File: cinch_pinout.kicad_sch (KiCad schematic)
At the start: 3 parts, among them J1 Conn, J2 Pinout

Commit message: Changed resistor footprint
Enables now both: SMD or throughhole resistor
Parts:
- added R1T1: 1k, Resistor_THT:R_Axial_DIN0207_L6.3mm_D2.5mm_P10.16mm_Horizontal, symbol Device:R
- J2: footprint (none) -> Connector_PinHeader_2.54mm:PinHeader_1x03_P2.54mm_Vertical
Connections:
- net +3V3: now also R1T1.1
- net AIN: now also R1T1.2
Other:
- moved on the sheet: R1
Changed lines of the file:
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@@
     (company "chof.org")
   )
+  (junction (at 140.97 62.23) (diameter 0) (color 0 0 0 0)
+  )
+  (junction (at 137.16 73.66) (diameter 0) (color 0 0 0 0)
+  )
   (junction (at 180.34 77.47) (diameter 0) (color 0 0 0 0)
   )
   (junction (at 176.53 71.12) (diameter 0) (color 0 0 0 0)
   )
-  (junction (at 140.97 73.66) (diameter 0) (color 0 0 0 0)
+  (junction (at 144.78 73.66) (diameter 0) (color 0 0 0 0)
   )
   (junction (at 132.08 73.66) (diameter 0) (color 0 0 0 0)
   )
+  (wire (pts (xy 180.34 78.74) (xy 180.34 77.47))
+    (stroke (width 0) (type default) (color 0 0 0 0))
+  )
+  (wire (pts (xy 137.16 62.23) (xy 137.16 63.5))
+    (stroke (width 0) (type default) (color 0 0 0 0))
+  )
+  (wire (pts (xy 144.78 71.12) (xy 144.78 73.66))
+    (stroke (width 0) (type default) (color 0 0 0 0))
+  )
+  (wire (pts (xy 137.16 73.66) (xy 144.78 73.66))
+    (stroke (width 0) (type default) (color 0 0 0 0))
+  )
+  (wire (pts (xy 144.78 73.66) (xy 148.59 73.66))
+    (stroke (width 0) (type default) (color 0 0 0 0))
+  )
+  (wire (pts (xy 132.08 73.66) (xy 137.16 73.66))
+    (stroke (width 0) (type default) (color 0 0 0 0))
+  )
+  (wire (pts (xy 144.78 62.23) (xy 144.78 63.5))
+    (stroke (width 0) (type default) (color 0 0 0 0))
+  )
+  (wire (pts (xy 182.88 66.04) (xy 182.88 71.12))
+    (stroke (width 0) (type default) (color 0 0 0 0))
+  )
+  (wire (pts (xy 111.76 76.2) (xy 111.76 69.85))
+    (stroke (width 0) (type default) (color 0 0 0 0))
+  )
+  (wire (pts (xy 140.97 62.23) (xy 144.78 62.23))
+    (stroke (width 0) (type default) (color 0 0 0 0))
+  )
+  (wire (pts (xy 140.97 62.23) (xy 137.16 62.23))
+    (stroke (width 0) (type default) (color 0 0 0 0))
+  )
+  (wire (pts (xy 180.34 76.2) (xy 171.45 76.2))
+    (stroke (width 0) (type default) (color 0 0 0 0))
+  )
+  (wire (pts (xy 134.62 76.2) (xy 134.62 92.71))
+    (stroke (width 0) (type default) (color 0 0 0 0))
+  )
+  (wire (pts (xy 132.08 69.85) (xy 132.08 73.66))
+    (stroke (width 0) (type default) (color 0 0 0 0))
+  )
+  (wire (pts (xy 176.53 71.12) (xy 171.45 71.12))
+    (stroke (width 0) (type default) (color 0 0 0 0))
+  )
+  (wire (pts (xy 111.76 69.85) (xy 132.08 69.85))
+    (stroke (width 0) (type default) (color 0 0 0 0))
+  )
   (wire (pts (xy 132.08 76.2) (xy 134.62 76.2))
     (stroke (width 0) (type default) (color 0 0 0 0))
   )
-  (wire (pts (xy 180.34 78.74) (xy 180.34 77.47))
-    (stroke (width 0) (type default) (color 0 0 0 0))
-  )
-  (wire (pts (xy 140.97 71.12) (xy 140.97 73.66))
-    (stroke (width 0) (type default) (color 0 0 0 0))
-  )
-  (wire (pts (xy 140.97 73.66) (xy 144.78 73.66))
-    (stroke (width 0) (type default) (color 0 0 0 0))
-  )
-  (wire (pts (xy 140.97 62.23) (xy 140.97 63.5))
-    (stroke (width 0) (type default) (color 0 0 0 0))
-  )
-  (wire (pts (xy 182.88 66.04) (xy 182.88 71.12))
-    (stroke (width 0) (type default) (color 0 0 0 0))
-  )
-  (wire (pts (xy 111.76 76.2) (xy 111.76 69.85))
-    (stroke (width 0) (type default) (color 0 0 0 0))
-  )
-  (wire (pts (xy 137.16 62.23) (xy 140.97 62.23))
-    (stroke (width 0) (type default) (color 0 0 0 0))
-  )
-  (wire (pts (xy 180.34 76.2) (xy 171.45 76.2))
-    (stroke (width 0) (type default) (color 0 0 0 0))
-  )
-  (wire (pts (xy 134.62 76.2) (xy 134.62 92.71))
-    (stroke (width 0) (type default) (color 0 0 0 0))
-  )
-  (wire (pts (xy 132.08 69.85) (xy 132.08 73.66))
-    (stroke (width 0) (type default) (color 0 0 0 0))
-  )
-  (wire (pts (xy 176.53 71.12) (xy 171.45 71.12))
-    (stroke (width 0) (type default) (color 0 0 0 0))
-  )
-  (wire (pts (xy 132.08 73.66) (xy 140.97 73.66))
-    (stroke (width 0) (type default) (color 0 0 0 0))
-  )
-  (wire (pts (xy 111.76 69.85) (xy 132.08 69.85))
-    (stroke (width 0) (type default) (color 0 0 0 0))
-  )
   (wire (pts (xy 182.88 71.12) (xy 176.53 71.12))
     (stroke (width 0) (type default) (color 0 0 0 0))
@@
   )
   (wire (pts (xy 180.34 77.47) (xy 180.34 76.2))
+    (stroke (width 0) (type default) (color 0 0 0 0))
+  )
+  (wire (pts (xy 137.16 71.12) (xy 137.16 73.66))
     (stroke (width 0) (type default) (color 0 0 0 0))
   )
@@
     )
   )
-  (global_label "AIN" (shape output) (at 144.78 73.66 0) (fields_autoplaced)
+  (global_label "AIN" (shape output) (at 148.59 73.66 0) (fields_autoplaced)
     (effects (font (size 1.27 1.27)) (justify left))
-    (property "Intersheet References" "${INTERSHEET_REFS}" (id 0) (at 150.2169 73.5806 0)
-      (effects (font (size 1.27 1.27)) (justify left) hide)
-    )
-  )
-  (symbol (lib_id "power:+3.3V") (at 137.16 62.23 0) (unit 1)
-    (in_bom yes) (on_board yes) (fields_autoplaced)
-    (property "Reference" "#PWR02" (id 0) (at 137.16 66.04 0)
-      (effects (font (size 1.27 1.27)) hide)
-    )
-    (property "Value" "+3.3V" (id 1) (at 137.16 57.15 0))
-    (property "Footprint" "" (id 2) (at 137.16 62.23 0)
-      (effects (font (size 1.27 1.27)) hide)
-    )
-    (property "Datasheet" "" (id 3) (at 137.16 62.23 0)
+    (property "Intersheet References" "${INTERSHEET_REFS}" (id 0) (at 154.0269 73.5806 0)
+      (effects (font (size 1.27 1.27)) (justify left) hide)
+    )
+  )
+  (symbol (lib_id "power:+3.3V") (at 140.97 62.23 0) (unit 1)
+    (in_bom yes) (on_board yes) (fields_autoplaced)
+    (property "Reference" "#PWR02" (id 0) (at 140.97 66.04 0)
+      (effects (font (size 1.27 1.27)) hide)
+    )
+    (property "Value" "+3.3V" (id 1) (at 140.97 57.15 0))
+    (property "Footprint" "" (id 2) (at 140.97 62.23 0)
+      (effects (font (size 1.27 1.27)) hide)
+    )
+    (property "Datasheet" "" (id 3) (at 140.97 62.23 0)
       (effects (font (size 1.27 1.27)) hide)
     )
@@
     (pin "1")
   )
-  (symbol (lib_id "Device:R") (at 140.97 67.31 0) (unit 1)
-    (in_bom yes) (on_board yes) (fields_autoplaced)
-    (property "Reference" "R1" (id 0) (at 143.51 66.0399 0)
-      (effects (font (size 1.27 1.27)) (justify left))
-    )
-    (property "Value" "1k" (id 1) (at 143.51 68.5799 0)
-      (effects (font (size 1.27 1.27)) (justify left))
-    )
-    (property "Footprint" "Resistor_SMD:R_0603_1608Metric_Pad0.98x0.95mm_HandSolder" (id 2) (at 139.192 67.31 90)
-      (effects (font (size 1.27 1.27)) hide)
-    )
-    (property "Datasheet" "~" (id 3) (at 140.97 67.31 0)
+  (symbol (lib_id "Device:R") (at 144.78 67.31 0) (unit 1)
+    (in_bom yes) (on_board yes) (fields_autoplaced)
+    (property "Reference" "R1" (id 0) (at 147.32 66.0399 0)
+      (effects (font (size 1.27 1.27)) (justify left))
+    )
+    (property "Value" "1k" (id 1) (at 147.32 68.5799 0)
+      (effects (font (size 1.27 1.27)) (justify left))
+    )
+    (property "Footprint" "Resistor_SMD:R_0603_1608Metric_Pad0.98x0.95mm_HandSolder" (id 2) (at 143.002 67.31 90)
+      (effects (font (size 1.27 1.27)) hide)
+    )
+    (property "Datasheet" "~" (id 3) (at 144.78 67.31 0)
       (effects (font (size 1.27 1.27)) hide)
     )
@@
     (pin "1")
   )
+  (symbol (lib_id "Device:R") (at 137.16 67.31 0) (unit 1)
+    (in_bom yes) (on_board yes) (fields_autoplaced)
+    (property "Reference" "R1T1" (id 0) (at 139.7 66.0399 0)
+      (effects (font (size 1.27 1.27)) (justify left))
+    )
+    (property "Value" "1k" (id 1) (at 139.7 68.5799 0)
+      (effects (font (size 1.27 1.27)) (justify left))
+    )
+    (property "Footprint" "Resistor_THT:R_Axial_DIN0207_L6.3mm_D2.5mm_P10.16mm_Horizontal" (id 2) (at 135.382 67.31 90)
+      (effects (font (size 1.27 1.27)) hide)
+    )
+    (property "Datasheet" "~" (id 3) (at 137.16 67.31 0)
+      (effects (font (size 1.27 1.27)) hide)
+    )
+    (pin "1")
+    (pin "2")
+  )
   (symbol (lib_id "Connector:Conn_01x03_Male") (at 166.37 73.66 0) (unit 1)
     (in_bom yes) (on_board yes) (fields_autoplaced)
     (property "Reference" "J2" (id 0) (at 167.005 66.04 0))
     (property "Value" "Pinout" (id 1) (at 167.005 68.58 0))
-    (property "Footprint" "" (id 2) (at 166.37 73.66 0)
+    (property "Footprint" "Connector_PinHeader_2.54mm:PinHeader_1x03_P2.54mm_Vertical" (id 2) (at 166.37 73.66 0)
       (effects (font (size 1.27 1.27)) hide)
     )
@@
       (reference "R1") (unit 1) (value "1k") (footprint "Resistor_SMD:R_0603_1608Metric_Pad0.98x0.95mm_HandSolder")
     )
-  )
+    (path "/88e5d2df-fb39-4d84-9641-41d1ac962e67"
+      (reference "R1T1") (unit 1) (value "1k") (footprint "Resistor_THT:R_Axial_DIN0207_L6.3mm_D2.5mm_P10.16mm_Horizontal")
+    )
+  )

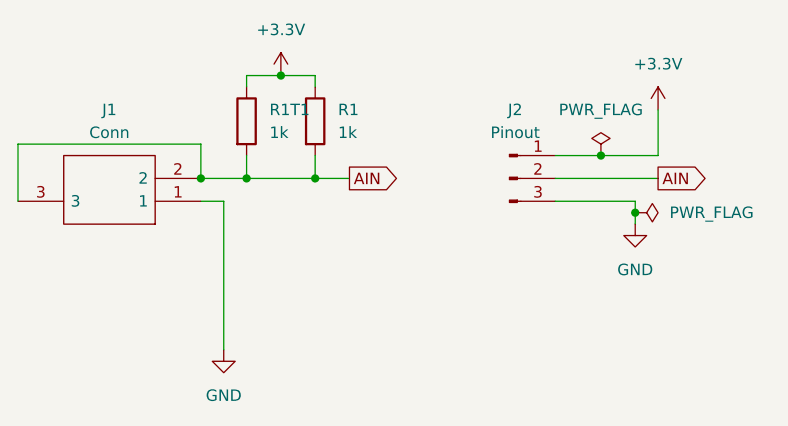
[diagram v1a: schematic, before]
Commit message: Updated template for KiCAD 7
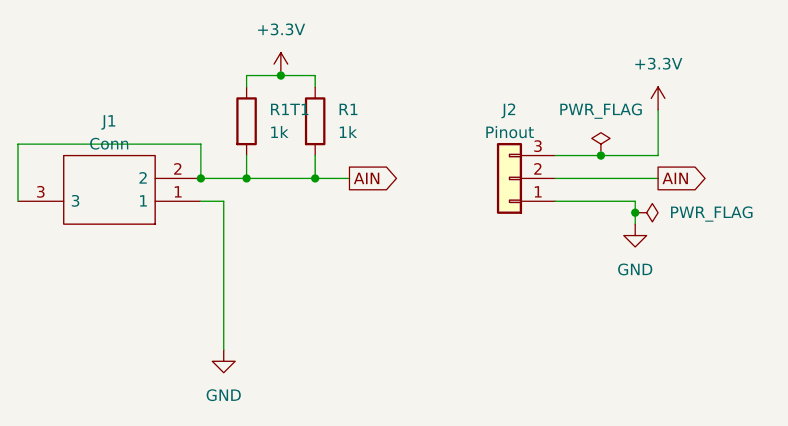
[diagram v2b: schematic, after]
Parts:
- J1: footprint footprints:MJ2509N -> MJ2509N; symbol MJ-2509N:MJ-2509N -> Connector_Audio:MJ-2509N
- J2: symbol Connector:Conn_01x03_Male -> Connector_Generic:Conn_01x03
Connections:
- net GND: now also J2.1 (Pin_1); no longer J2.3 (Pin_3)
- net +3V3 renamed +3.3V
- net +3.3V: now also J2.3 (Pin_3); no longer J2.1 (Pin_1)
